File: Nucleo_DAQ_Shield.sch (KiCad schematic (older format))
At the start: 10 parts

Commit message: Added analog buffers and connection for motor/encoder
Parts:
- added J?: CONN_01X06, symbol CONN_01X06
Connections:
- net labels added: ENCODER_A, ENCODER_B, MOTOR+, MOTOR-
- wire segments 16 -> 19
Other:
- note added: "Motor from http://www.robotshop.com/en/6v-301-530rpm-micro-metal-gearmotor-encoder.html"
- note added: "how much current does the encoder draw????"
- moved on the sheet: J?, U?A, U?B
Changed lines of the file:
@@
 L TL072 U?
 U 1 1 5954222C
-P 2800 3800
-F 0 "U?" H 2800 4000 50  0000 L CNN
-F 1 "TL072" H 2800 3600 50  0000 L CNN
-F 2 "" H 2800 3800 50  0001 C CNN
-F 3 "" H 2800 3800 50  0001 C CNN
-	1    2800 3800
+P 2600 5250
+F 0 "U?" H 2600 5450 50  0000 L CNN
+F 1 "TL072" H 2600 5050 50  0000 L CNN
+F 2 "" H 2600 5250 50  0001 C CNN
+F 3 "" H 2600 5250 50  0001 C CNN
+	1    2600 5250
 	1    0    0    -1
 $EndComp
@@
 L TL072 U?
 U 2 1 5954224F
-P 2850 5500
-F 0 "U?" H 2850 5700 50  0000 L CNN
-F 1 "TL072" H 2850 5300 50  0000 L CNN
-F 2 "" H 2850 5500 50  0001 C CNN
-F 3 "" H 2850 5500 50  0001 C CNN
-	2    2850 5500
+P 2650 6950
+F 0 "U?" H 2650 7150 50  0000 L CNN
+F 1 "TL072" H 2650 6750 50  0000 L CNN
+F 2 "" H 2650 6950 50  0001 C CNN
+F 3 "" H 2650 6950 50  0001 C CNN
+	2    2650 6950
 	1    0    0    -1
 $EndComp
@@
 L CONN_COAXIAL J?
 U 1 1 59542D8D
-P 2100 5400
-F 0 "J?" H 2110 5520 50  0000 C CNN
-F 1 "CONN_COAXIAL" V 2215 5400 50  0000 C CNN
-F 2 "" H 2100 5400 50  0001 C CNN
-F 3 "" H 2100 5400 50  0001 C CNN
-	1    2100 5400
+P 1900 6850
+F 0 "J?" H 1910 6970 50  0000 C CNN
+F 1 "CONN_COAXIAL" V 2015 6850 50  0000 C CNN
+F 2 "" H 1900 6850 50  0001 C CNN
+F 3 "" H 1900 6850 50  0001 C CNN
+	1    1900 6850
 	-1   0    0    -1
 $EndComp
@@
 L +3.3V #PWR?
 U 1 1 59543308
-P 2750 5200
-F 0 "#PWR?" H 2750 5050 50  0001 C CNN
-F 1 "+3.3V" H 2750 5340 50  0000 C CNN
-F 2 "" H 2750 5200 50  0001 C CNN
-F 3 "" H 2750 5200 50  0001 C CNN
-	1    2750 5200
+P 2550 6650
+F 0 "#PWR?" H 2550 6500 50  0001 C CNN
+F 1 "+3.3V" H 2550 6790 50  0000 C CNN
+F 2 "" H 2550 6650 50  0001 C CNN
+F 3 "" H 2550 6650 50  0001 C CNN
+	1    2550 6650
 	1    0    0    -1
 $EndComp
@@
 L GNDA #PWR?
 U 1 1 5954333D
-P 2750 5800
-F 0 "#PWR?" H 2750 5550 50  0001 C CNN
-F 1 "GNDA" H 2750 5650 50  0000 C CNN
-F 2 "" H 2750 5800 50  0001 C CNN
-F 3 "" H 2750 5800 50  0001 C CNN
-	1    2750 5800
+P 2550 7250
+F 0 "#PWR?" H 2550 7000 50  0001 C CNN
+F 1 "GNDA" H 2550 7100 50  0000 C CNN
+F 2 "" H 2550 7250 50  0001 C CNN
+F 3 "" H 2550 7250 50  0001 C CNN
+	1    2550 7250
 	1    0    0    -1
 $EndComp
@@
 L +3.3V #PWR?
 U 1 1 5954345E
-P 2700 3500
-F 0 "#PWR?" H 2700 3350 50  0001 C CNN
-F 1 "+3.3V" H 2700 3640 50  0000 C CNN
-F 2 "" H 2700 3500 50  0001 C CNN
-F 3 "" H 2700 3500 50  0001 C CNN
-	1    2700 3500
+P 2500 4950
+F 0 "#PWR?" H 2500 4800 50  0001 C CNN
+F 1 "+3.3V" H 2500 5090 50  0000 C CNN
+F 2 "" H 2500 4950 50  0001 C CNN
+F 3 "" H 2500 4950 50  0001 C CNN
+	1    2500 4950
 	1    0    0    -1
 $EndComp
@@
 L GNDA #PWR?
 U 1 1 5954348A
-P 2700 4100
-F 0 "#PWR?" H 2700 3850 50  0001 C CNN
-F 1 "GNDA" H 2700 3950 50  0000 C CNN
-F 2 "" H 2700 4100 50  0001 C CNN
-F 3 "" H 2700 4100 50  0001 C CNN
-	1    2700 4100
+P 2500 5550
+F 0 "#PWR?" H 2500 5300 50  0001 C CNN
+F 1 "GNDA" H 2500 5400 50  0000 C CNN
+F 2 "" H 2500 5550 50  0001 C CNN
+F 3 "" H 2500 5550 50  0001 C CNN
+	1    2500 5550
 	1    0    0    -1
 $EndComp
@@
 L CONN_01X02 J?
 U 1 1 59543763
-P 3600 3850
-F 0 "J?" H 3600 4000 50  0000 C CNN
-F 1 "CONN_01X02" V 3700 3850 50  0000 C CNN
-F 2 "" H 3600 3850 50  0001 C CNN
-F 3 "" H 3600 3850 50  0001 C CNN
-	1    3600 3850
+P 3400 5300
+F 0 "J?" H 3400 5450 50  0000 C CNN
+F 1 "CONN_01X02" V 3500 5300 50  0000 C CNN
+F 2 "" H 3400 5300 50  0001 C CNN
+F 3 "" H 3400 5300 50  0001 C CNN
+	1    3400 5300
 	1    0    0    -1
 $EndComp
 Wire Wire Line
-	3100 3800 3400 3800
+	2900 5250 3200 5250
 Wire Wire Line
-	3200 3800 3200 4200
+	3000 5250 3000 5650
 Wire Wire Line
-	3200 4200 2400 4200
+	3000 5650 2200 5650
 Wire Wire Line
-	2400 4200 2400 3900
+	2200 5650 2200 5350
 Wire Wire Line
-	2400 3900 2500 3900
+	2200 5350 2300 5350
 Wire Wire Line
-	3150 5500 3400 5500
+	2950 6950 3200 6950
 Wire Wire Line
-	3250 5500 3250 5900
+	3050 6950 3050 7350
 Wire Wire Line
-	3250 5900 2450 5900
+	3050 7350 2250 7350
 Wire Wire Line
-	2450 5900 2450 5600
+	2250 7350 2250 7050
 Wire Wire Line
-	2450 5600 2550 5600
+	2250 7050 2350 7050
 Wire Wire Line
 	1400 1300 1400 1200
@@
 	1600 1100 1600 1300
 Connection ~ 1600 1200
-Connection ~ 3200 3800
+Connection ~ 3000 5250
 $Comp
 L GNDA #PWR?
 U 1 1 595438C3
-P 3400 3900
-F 0 "#PWR?" H 3400 3650 50  0001 C CNN
-F 1 "GNDA" H 3400 3750 50  0000 C CNN
-F 2 "" H 3400 3900 50  0001 C CNN
-F 3 "" H 3400 3900 50  0001 C CNN
-	1    3400 3900
+P 3200 5350
+F 0 "#PWR?" H 3200 5100 50  0001 C CNN
+F 1 "GNDA" H 3200 5200 50  0000 C CNN
+F 2 "" H 3200 5350 50  0001 C CNN
+F 3 "" H 3200 5350 50  0001 C CNN
+	1    3200 5350
 	1    0    0    -1
 $EndComp
 Wire Wire Line
-	2500 3700 2100 3700
-Text Label 2100 3700 2    60   ~ 0
+	2300 5150 1900 5150
+Text Label 1900 5150 2    60   ~ 0
 GAIN
 Wire Wire Line
-	2250 5400 2550 5400
+	2050 6850 2350 6850
 $Comp
 L GNDA #PWR?
 U 1 1 59543B89
-P 2100 5600
-F 0 "#PWR?" H 2100 5350 50  0001 C CNN
-F 1 "GNDA" H 2100 5450 50  0000 C CNN
-F 2 "" H 2100 5600 50  0001 C CNN
-F 3 "" H 2100 5600 50  0001 C CNN
-	1    2100 5600
+P 1900 7050
+F 0 "#PWR?" H 1900 6800 50  0001 C CNN
+F 1 "GNDA" H 1900 6900 50  0000 C CNN
+F 2 "" H 1900 7050 50  0001 C CNN
+F 3 "" H 1900 7050 50  0001 C CNN
+	1    1900 7050
 	1    0    0    -1
 $EndComp
-Text Label 3200 3800 1    60   ~ 0
+Text Label 3000 5250 1    60   ~ 0
 GAIN_buffered
-Text Label 2350 5400 1    60   ~ 0
+Text Label 2150 6850 1    60   ~ 0
 ENVLP
-Text Label 3400 5500 0    60   ~ 0
+Text Label 3200 6950 0    60   ~ 0
 ENVLP_buffered
 Wire Notes Line
-	1700 3100 3900 3100
+	1500 4550 3700 4550
 Wire Notes Line
-	3900 3100 3900 4400
+	3700 4550 3700 5850
 Wire Notes Line
-	3900 4400 1700 4400
+	3700 5850 1500 5850
 Wire Notes Line
-	1700 4400 1700 3100
-Text Notes 1800 3050 0    60   ~ 0
+	1500 5850 1500 4550
+Text Notes 1600 4500 0    60   ~ 0
 Output buffer for gain signal
-Connection ~ 3250 5500
+Connection ~ 3050 6950
 Wire Notes Line
-	1700 4900 4300 4900
+	1500 6350 4100 6350
 Wire Notes Line
-	4300 4900 4300 6200
+	4100 6350 4100 7650
 Wire Notes Line
-	4300 6200 1700 6200
+	4100 7650 1500 7650
 Wire Notes Line
-	1700 6200 1700 4900
-Text Notes 1750 4850 0    60   ~ 0
+	1500 7650 1500 6350
+Text Notes 1550 6300 0    60   ~ 0
 Input buffer for envelope signal
-Text Notes 1750 3850 0    40   ~ 0
+Text Notes 1550 5300 0    40   ~ 0
 from DAC output
-Text Notes 3450 5650 0    40   ~ 0
+Text Notes 3250 7100 0    40   ~ 0
 to ADC input
 $Bitmap
-Pos 6000 3150
+Pos 1700 3300
 Scale 1.000000
 Data
@@
 EndData
 $EndBitmap
+$Comp
+L CONN_01X06 J?
+U 1 1 595A8E5A
+P 3000 3250
+F 0 "J?" H 3000 3600 50  0000 C CNN
+F 1 "CONN_01X06" V 3100 3250 50  0000 C CNN
+F 2 "" H 3000 3250 50  0001 C CNN
+F 3 "" H 3000 3250 50  0001 C CNN
+	1    3000 3250
+	-1   0    0    -1
+$EndComp
+Text Notes 750  2800 0    30   ~ 0
+Motor from http://www.robotshop.com/en/6v-301-530rpm-micro-metal-gearmotor-encoder.html
+Text Label 3200 3000 0    30   ~ 0
+MOTOR+
+Text Label 3200 3500 0    30   ~ 0
+MOTOR-
+Text Label 3200 3200 0    30   ~ 0
+ENCODER_A
+Text Label 3200 3300 0    30   ~ 0
+ENCODER_B
+$Comp
+L +3.3V #PWR?
+U 1 1 595A94F2
+P 3600 3000
+F 0 "#PWR?" H 3600 2850 50  0001 C CNN
+F 1 "+3.3V" H 3600 3140 50  0000 C CNN
+F 2 "" H 3600 3000 50  0001 C CNN
+F 3 "" H 3600 3000 50  0001 C CNN
+	1    3600 3000
+	1    0    0    -1
+$EndComp
+Wire Wire Line
+	3200 3100 3600 3100
+Wire Wire Line
+	3600 3100 3600 3000
+$Comp
+L GNDD #PWR?
+U 1 1 595A9604
+P 3600 3400
+F 0 "#PWR?" H 3600 3150 50  0001 C CNN
+F 1 "GNDD" H 3600 3250 50  0000 C CNN
+F 2 "" H 3600 3400 50  0001 C CNN
+F 3 "" H 3600 3400 50  0001 C CNN
+	1    3600 3400
+	1    0    0    -1
+$EndComp
+Wire Wire Line
+	3200 3400 3600 3400
+Text Notes 1650 3850 0    50   Italic 10
+how much current does the encoder draw????
 $EndSCHEMATC

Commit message: Added voltage regulators and updated encoder connections
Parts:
- removed U?: 4050, symbol 4050
- removed U?: LM1117-3.3, symbol LM1117-3.3
- added C1: 10uF tant, symbol CP_Small
- added C2: 0.33uF, symbol C_Small
- added C3: 100nF, symbol C_Small
- added C4: 1uF cer, symbol C_Small
- added D1: green, symbol LED_Small
- added J1: CONN_01X02, symbol CONN_01X02
- added J5: CONN_01X06, symbol CONN_01X06
- added JP? (x2): Jumper_NC_Dual, symbol Jumper_NC_Dual
- added R1: 1k, symbol R_Small
- added U3: TLV70233DBV, TO_SOT_Packages_SMD:SOT-23-5, symbol TLV70233DBV
- gave numbers to parts that had none: 6
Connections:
- net labels added: +3.3VA, +5V, +5VA, +5VD, CUI_encoder_A, CUI_encoder_B, CUI_encoder_X, Motor_encoder_A, Motor_encoder_B, Vbat
- wire segments 19 -> 35
- no-connect marks 0 -> 1
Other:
- note added: "3.3V 300mA regulator"
- note added: "CUI capacitive encoder (5V)"
- note added: "Motor speed control"
- note added: "Nucleo connectors"
- note removed: "how much current does the encoder draw????"
- moved on the sheet: J2, J3, J4, U1A, U1B, U2, U4A, U4B, U4C

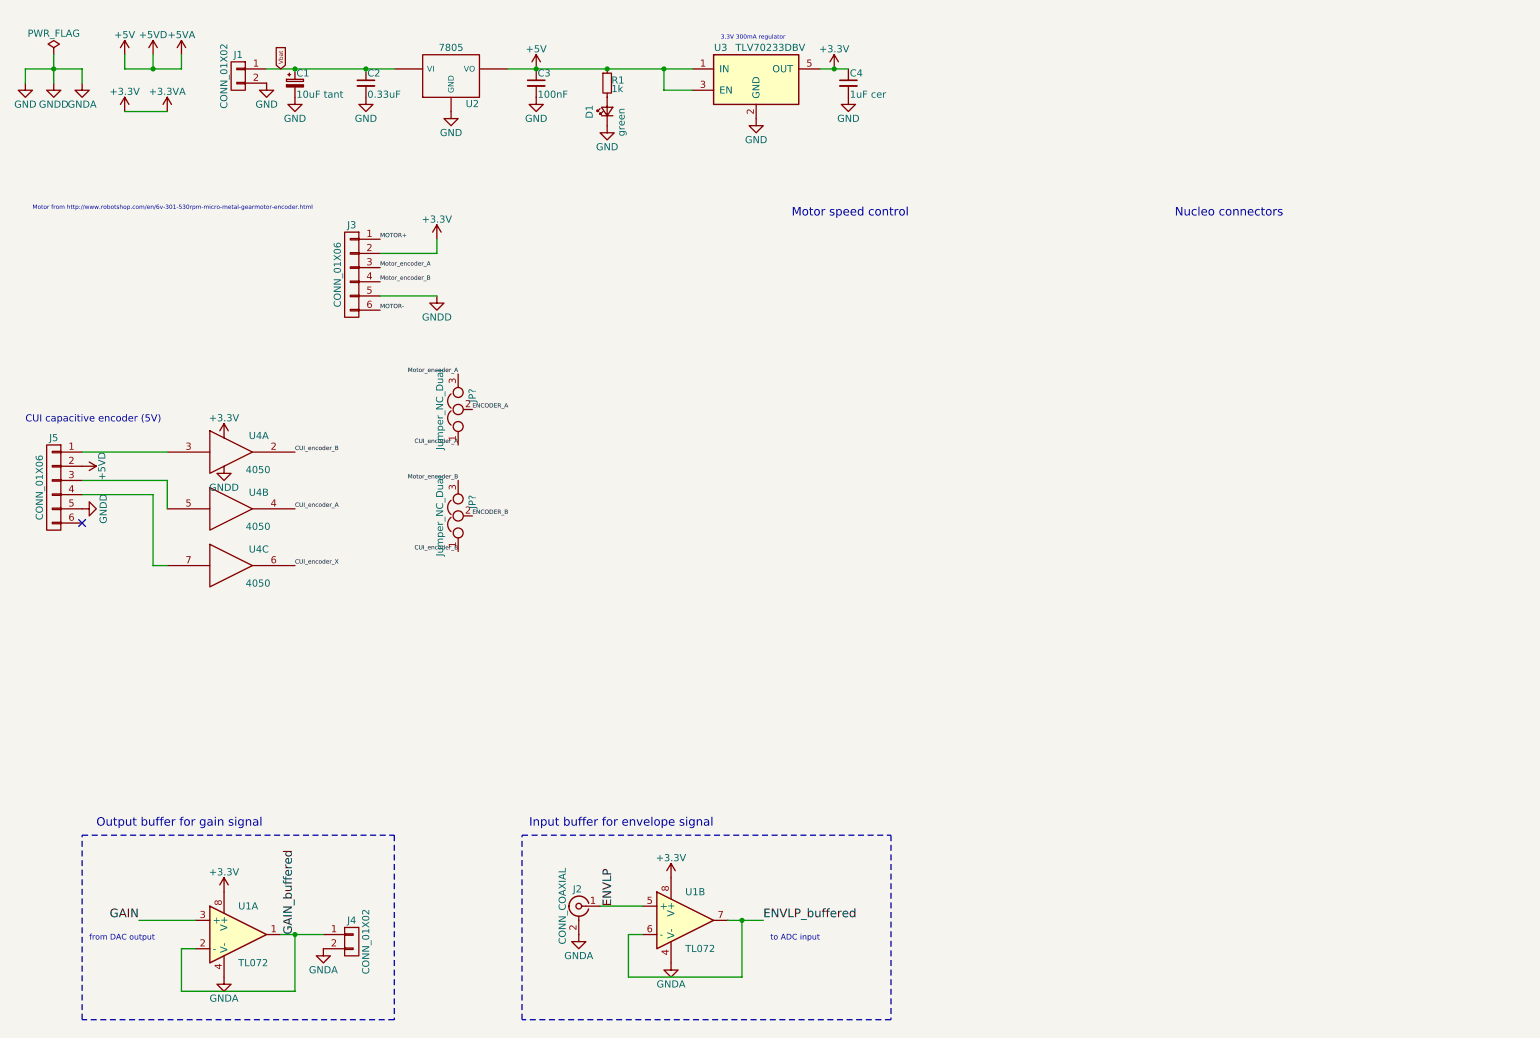
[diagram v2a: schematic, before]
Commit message: Added Overvoltage Protection for envelope input buffer and jumpers to choose between motor encoder vs CUI encoder
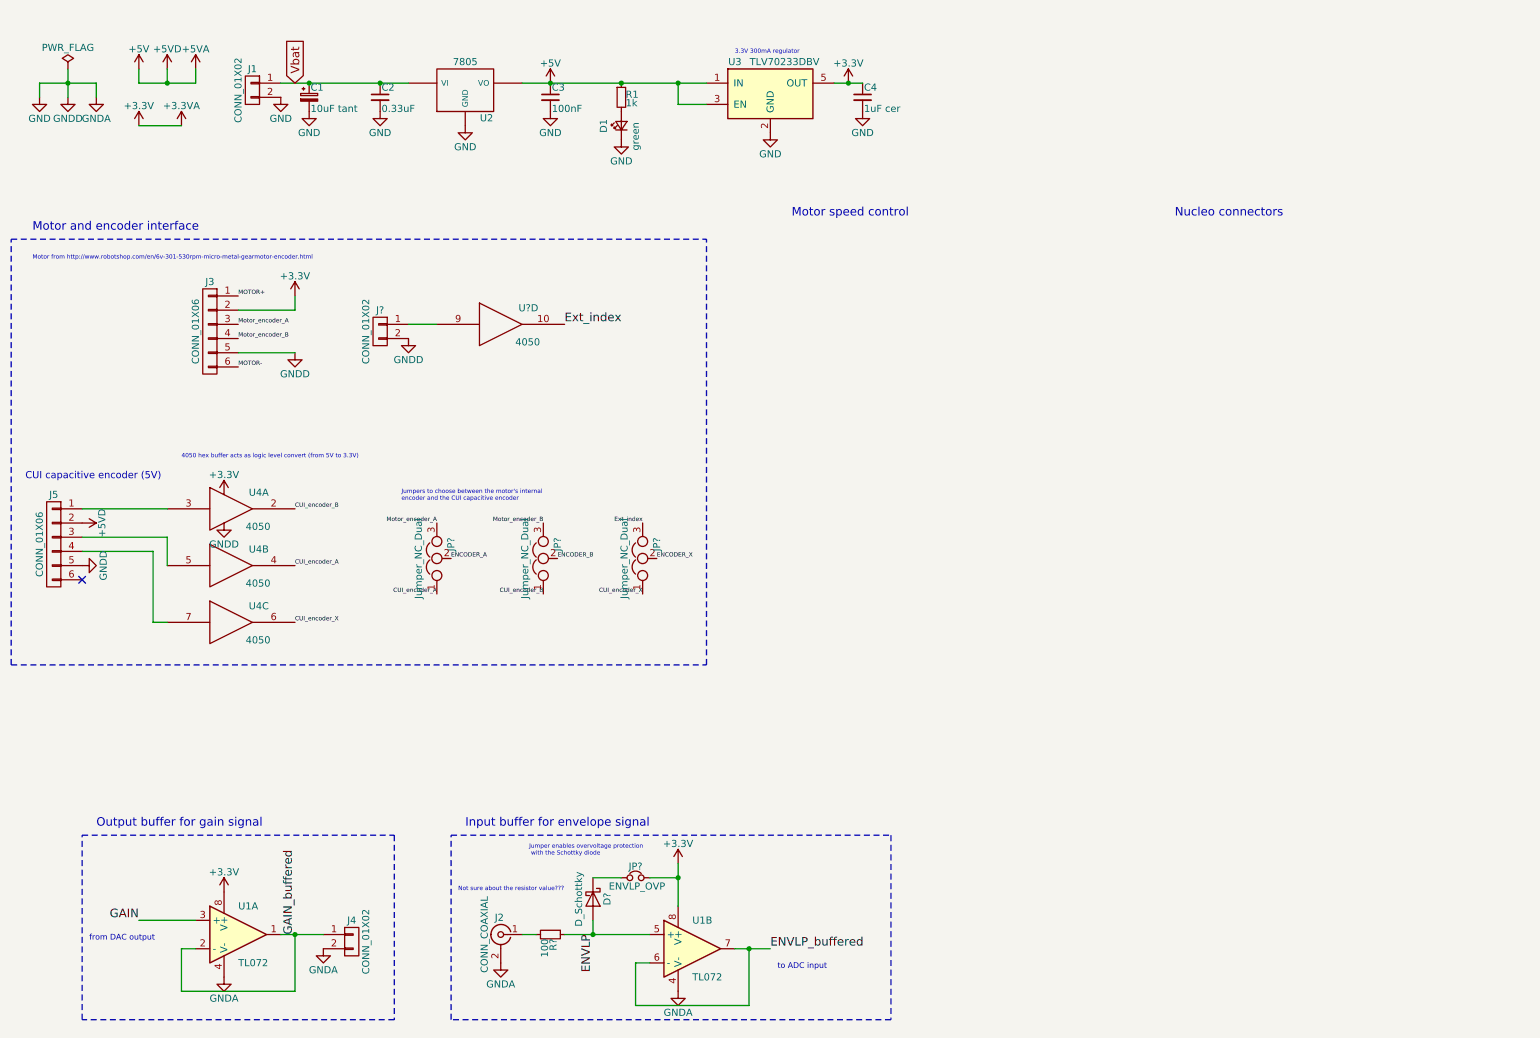
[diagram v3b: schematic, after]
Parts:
- added D?: D_Schottky, symbol D_Schottky
- added J?: CONN_01X02, symbol CONN_01X02
- added JP?: ENVLP_OVP, symbol Jumper_NC_Small
- added JP?: Jumper_NC_Dual, symbol Jumper_NC_Dual
- added R?: 100, symbol R_Small
- added U?: 4050, symbol 4050
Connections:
- net +3.3VA: now also JP?.2, U?.1 (VCC)
- net CUI_encoder_X: now also JP?.1
- net ENVLP: now also D?.2 (A), R?.1; no longer J2.1 (In)
- net GND: now also J?.2 (P2), U?.8 (VSS)
- new net: J2.1 (In), R?.2
- new net: D?.1 (K), JP?.1
- new net: J?.1 (P1), U?.9
- new net ENCODER_X: JP?.2
- new net Ext_index: JP?.3, U?.10
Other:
- note added: "4050 hex buffer acts as logic level convert (from 5V to 3.3V)"
- note added: "Jumper enables overvoltage protection\n with the Schottky diode"
- note added: "Jumpers to choose between the motor's internal \nencoder and the CUI capacitive encoder"
- note added: "Motor and encoder interface"
- note added: "Not sure about the resistor value???"
- moved on the sheet: C1, C2, C3, C4, D1, J1, J2, J3, J5, JP?, R1, U1B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
